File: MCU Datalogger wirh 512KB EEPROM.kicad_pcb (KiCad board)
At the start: 2 copper layers, 56.3 x 48.7 mm, 30 parts, among them IC1 ATMEGA328P-AU, J1 Conn_01x04_Pin, J2 Conn_01x04_Pin, J3 Conn_01x09_Pin, J4 Conn_02x03_Odd_Even, U1 24LC1025, U2 24LC1025, U3 DS1137S+, Y1 16 MHz, Y2 32.768 KHz

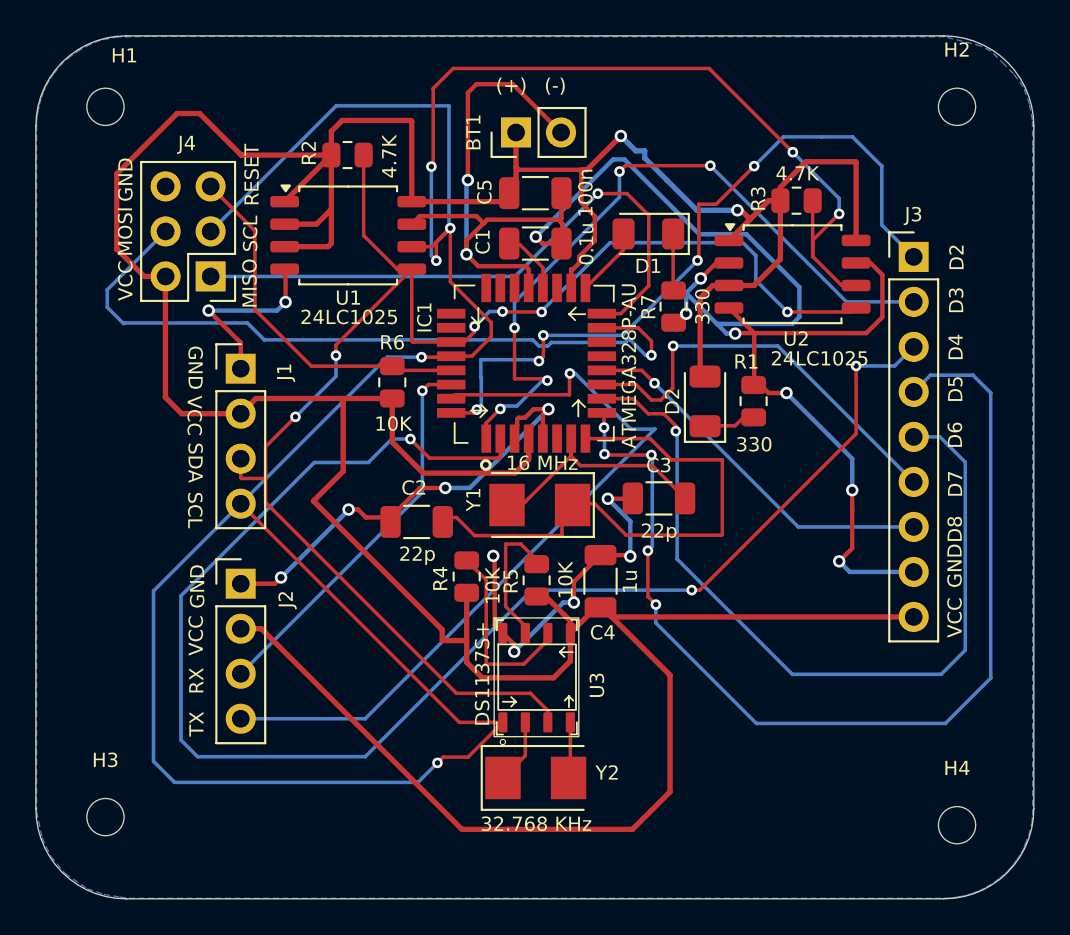
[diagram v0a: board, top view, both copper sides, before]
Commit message: Done the routing of the 4-layer PCB layout.
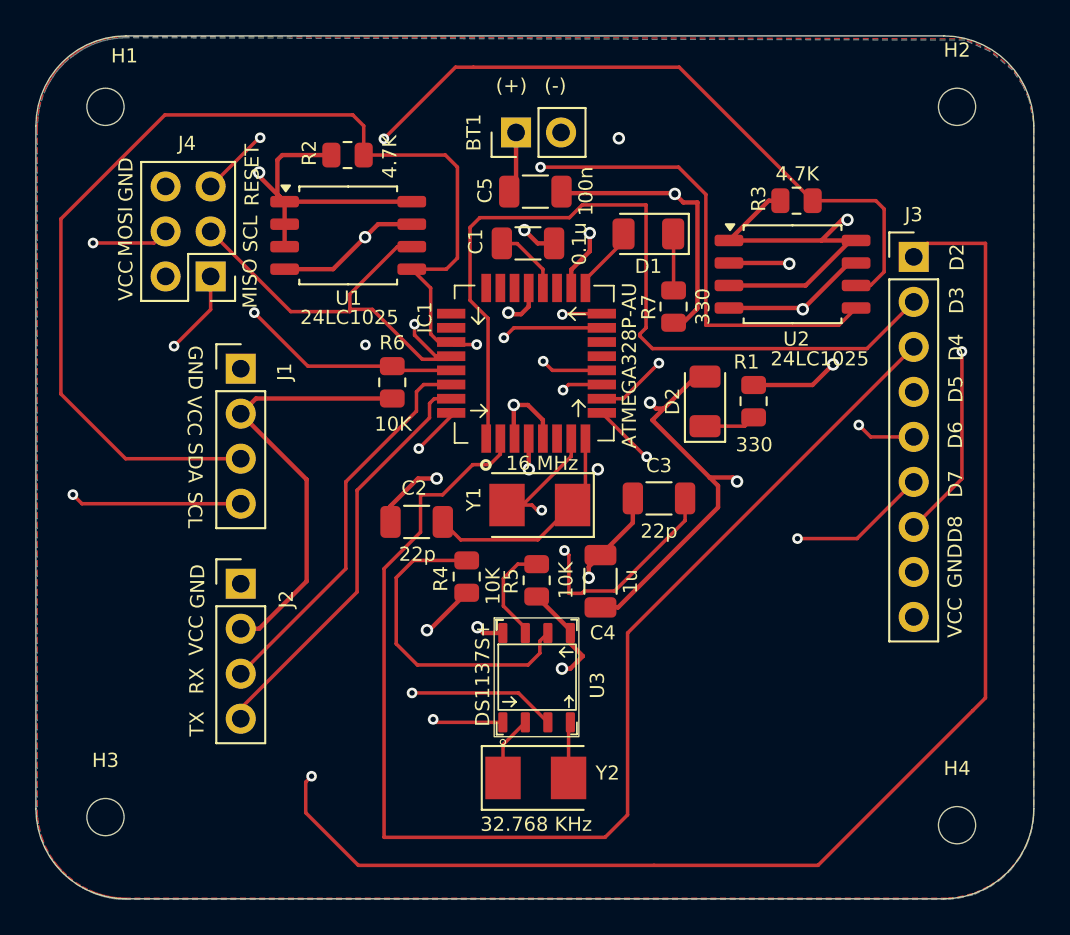
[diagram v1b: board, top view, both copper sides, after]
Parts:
- moved C1 0.42 mm to (135.5, 86.4)
- moved C5 0.09 mm to (135.9, 83.5)
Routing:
- net /D2: track 41.4 -> 99.5 mm, vias 5 -> 2
- net GND: track 165.2 -> 108.5 mm, vias 20 -> 11
- net /SDA: track 82.9 -> 137.3 mm, vias 6 -> 3
- net /D5: track 58.6 -> 20.1 mm, vias 5 -> 1
- net /Vcc: track 237.0 -> 199.7 mm, vias 2 -> 10
- net /D8: track 21.3 -> 54.3 mm, vias 1 -> 2
- net /D6: track 46.0 -> 20.9 mm, vias 1 -> 2
- net /TX: track 44.4 -> 23.5 mm, vias 1 -> 0
- net Net-(IC1-PB7): track 31.8 -> 12.6 mm
- net /D4: track 84.9 -> 73.9 mm, vias 3 -> 0
- net /RESET: track 20.6 -> 30.4 mm, vias 0 -> 2
- net Net-(IC1-PB6): track 14.2 -> 22.7 mm, vias 0 -> 2
- net Net-(U3-!INTA): track 10.7 -> 18.3 mm
- net /MOSI: track 41.7 -> 48.0 mm, vias 1 -> 2
- net /D7: track 23.8 -> 30.1 mm, vias 1 -> 2
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- added copper zone on F.Cu, net /Vcc
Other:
- copper layers 2 -> 4

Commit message: Improved the wiring for potential signal interferences.
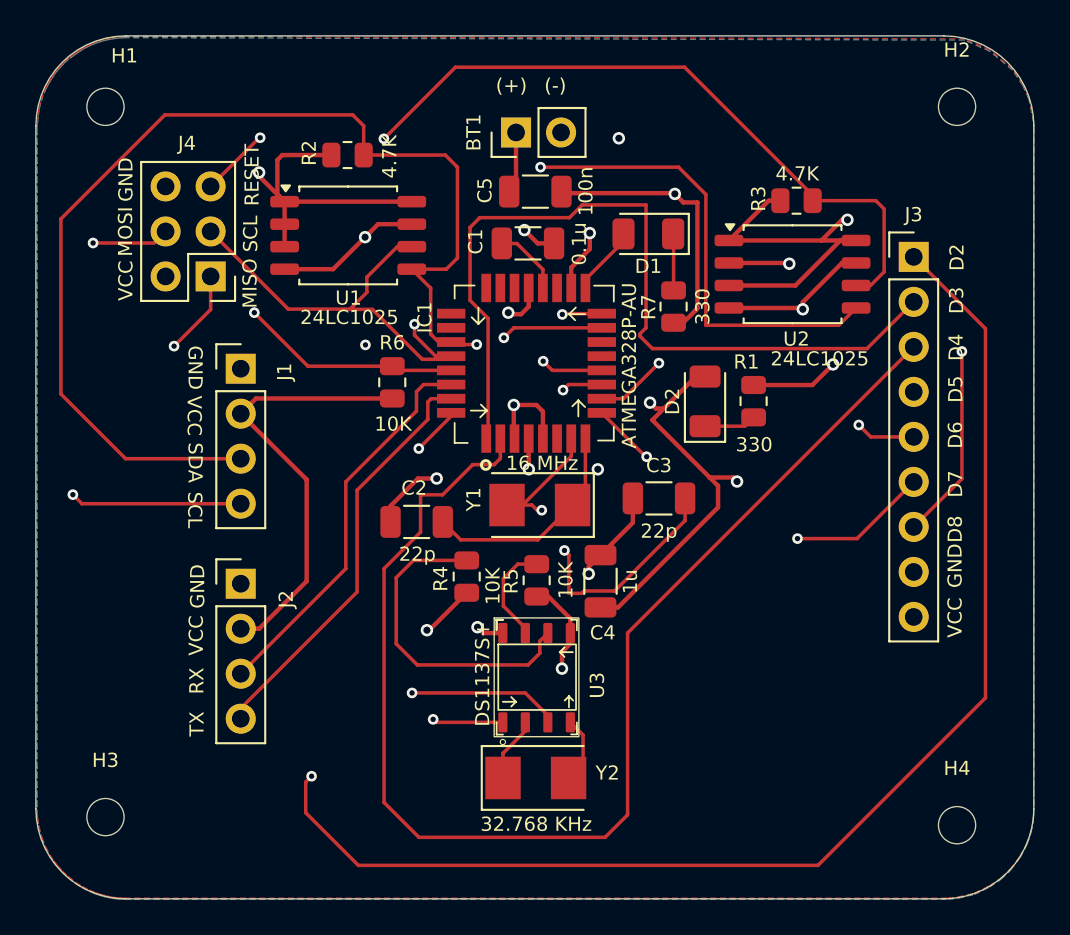
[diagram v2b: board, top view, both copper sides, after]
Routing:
- net /D2: track 99.5 -> 96.0 mm
- net /D4: track 73.9 -> 72.9 mm
- net Net-(U3-X2): track 3.18 -> 3.77 mm
- net GND: track 108.5 -> 109.0 mm
